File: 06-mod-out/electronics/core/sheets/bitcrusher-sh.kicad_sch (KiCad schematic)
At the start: 22 parts, among them Q2 2N3819, U1 TL072, U2 TL072

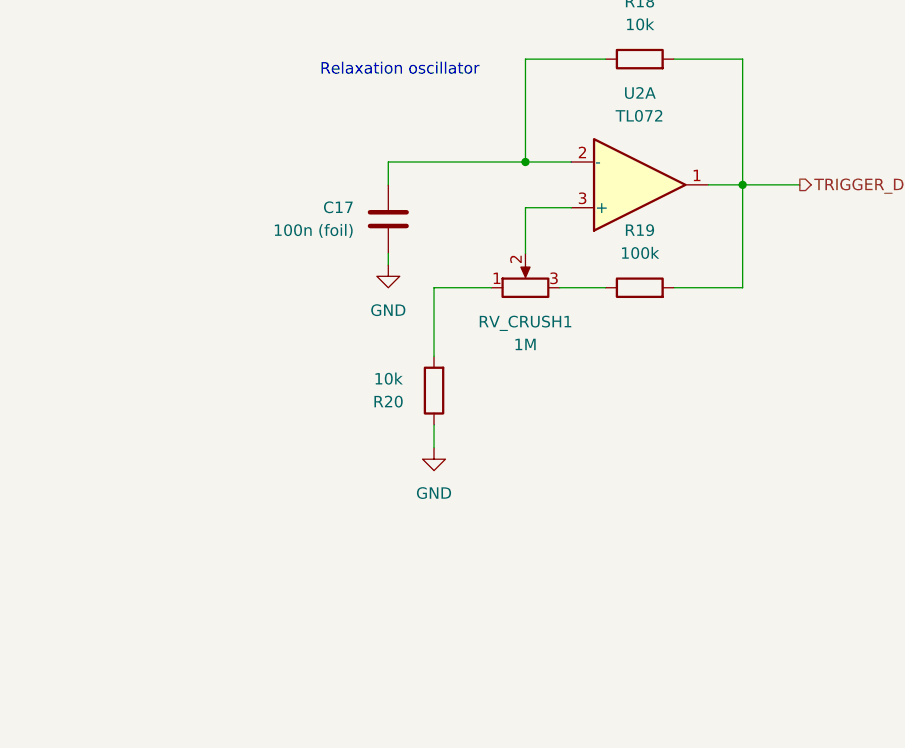
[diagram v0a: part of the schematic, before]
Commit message: Started Mod/Output PCB
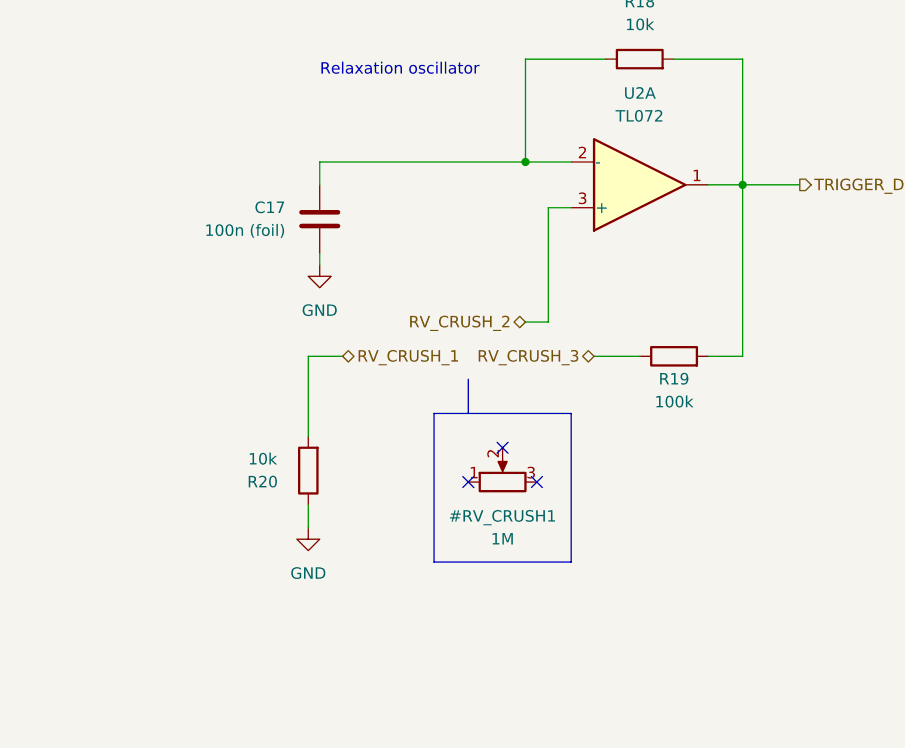
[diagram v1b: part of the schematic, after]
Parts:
- Q2: footprint Package_TO_SOT_THT:TO-92 -> Package_TO_SOT_THT:TO-92_Inline_Wide
- R17: LCSC (none) -> C21190
- R18, R20: LCSC (none) -> C25804
- R19, R21, R22, R23: LCSC (none) -> C25803
- renumbered RV_CRUSH1 to #RV_CRUSH1
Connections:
- net at #RV_CRUSH1.3: no longer R19.1
- net at #RV_CRUSH1.2: no longer U2.3 (+)
- net at #RV_CRUSH1.1: no longer R20.2
- new net RV_CRUSH_1: R20.2
- new net RV_CRUSH_2: U2.3 (+)
- new net RV_CRUSH_3: R19.1
- no-connect marks 0 -> 3
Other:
- moved on the sheet: C17, R19, R20
